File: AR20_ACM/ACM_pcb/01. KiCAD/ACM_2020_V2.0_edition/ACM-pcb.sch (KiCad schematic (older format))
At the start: 32 parts, among them IC1 MCP25625T-E_ML, J1 TC2030-MCP-NL, P1 Conn_02x15_Odd_Even, Q1 Q_PMOS_DMP3099L-13, U1 ATmega328P-AU, U3 NCV890430MW50TXG, Y1 16.0Mhz

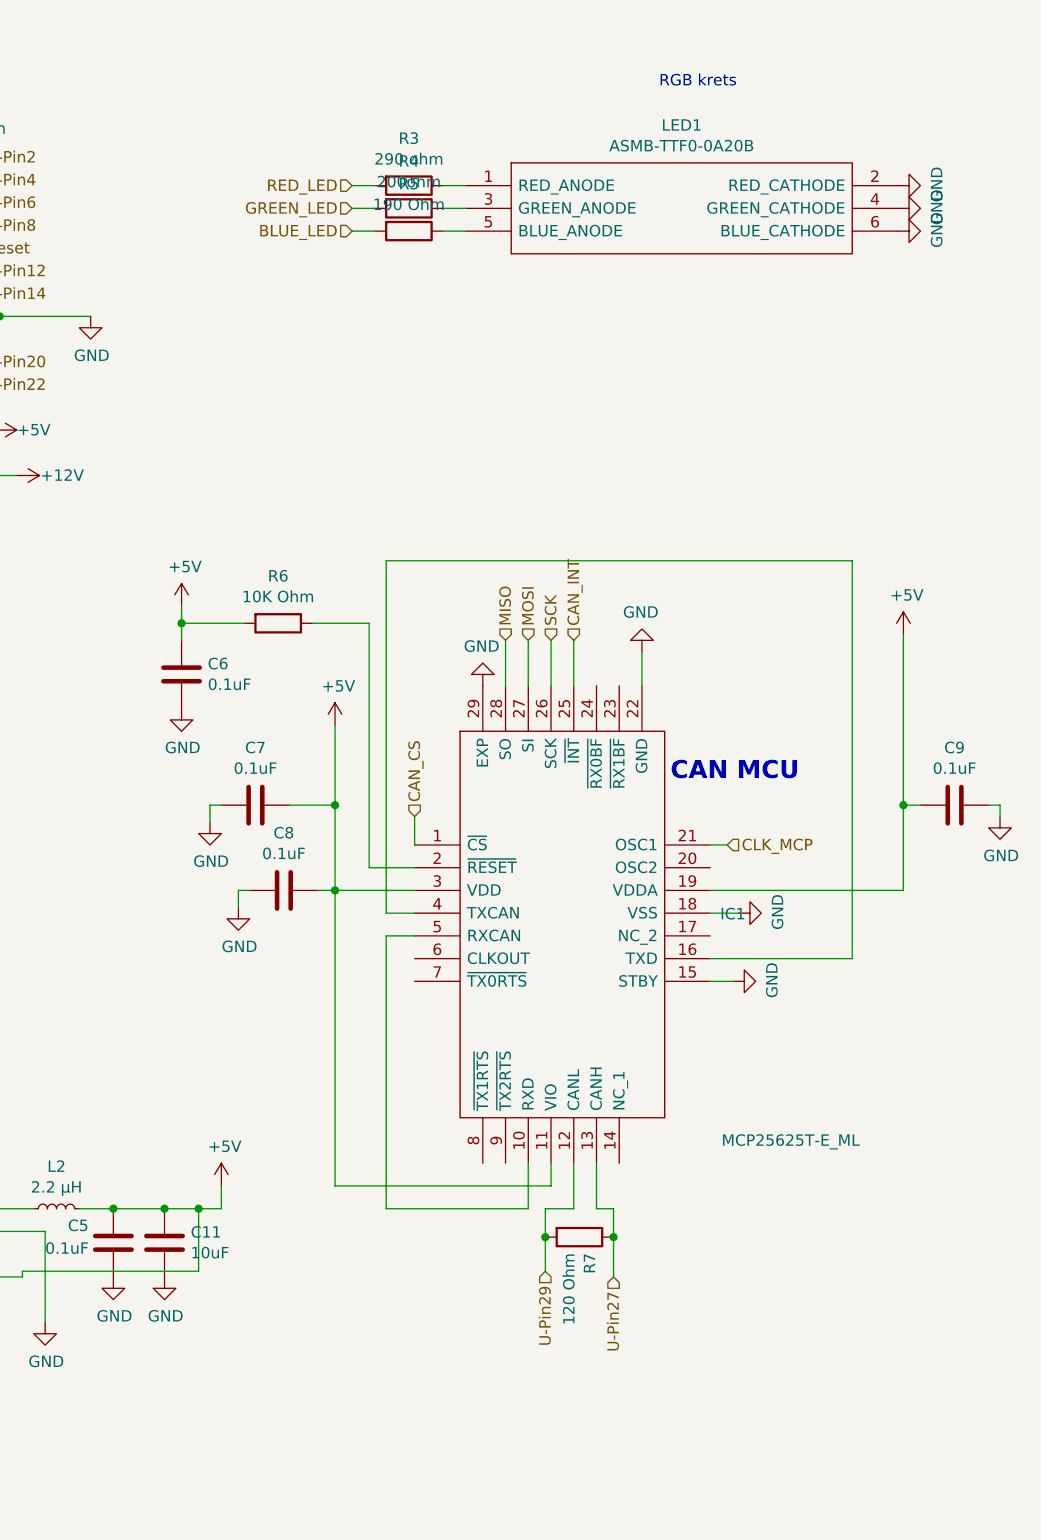
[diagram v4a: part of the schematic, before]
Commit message: NOT COMPLETE V3.0 ACM
This is the beginning of the V3.0 ACM. With added CAN FD transiver and CAN FD controller. 
To fix: 
Chagne CAN FD transciver to a SOCI version 
Place all capacitors in a good location. 
Board cleanup
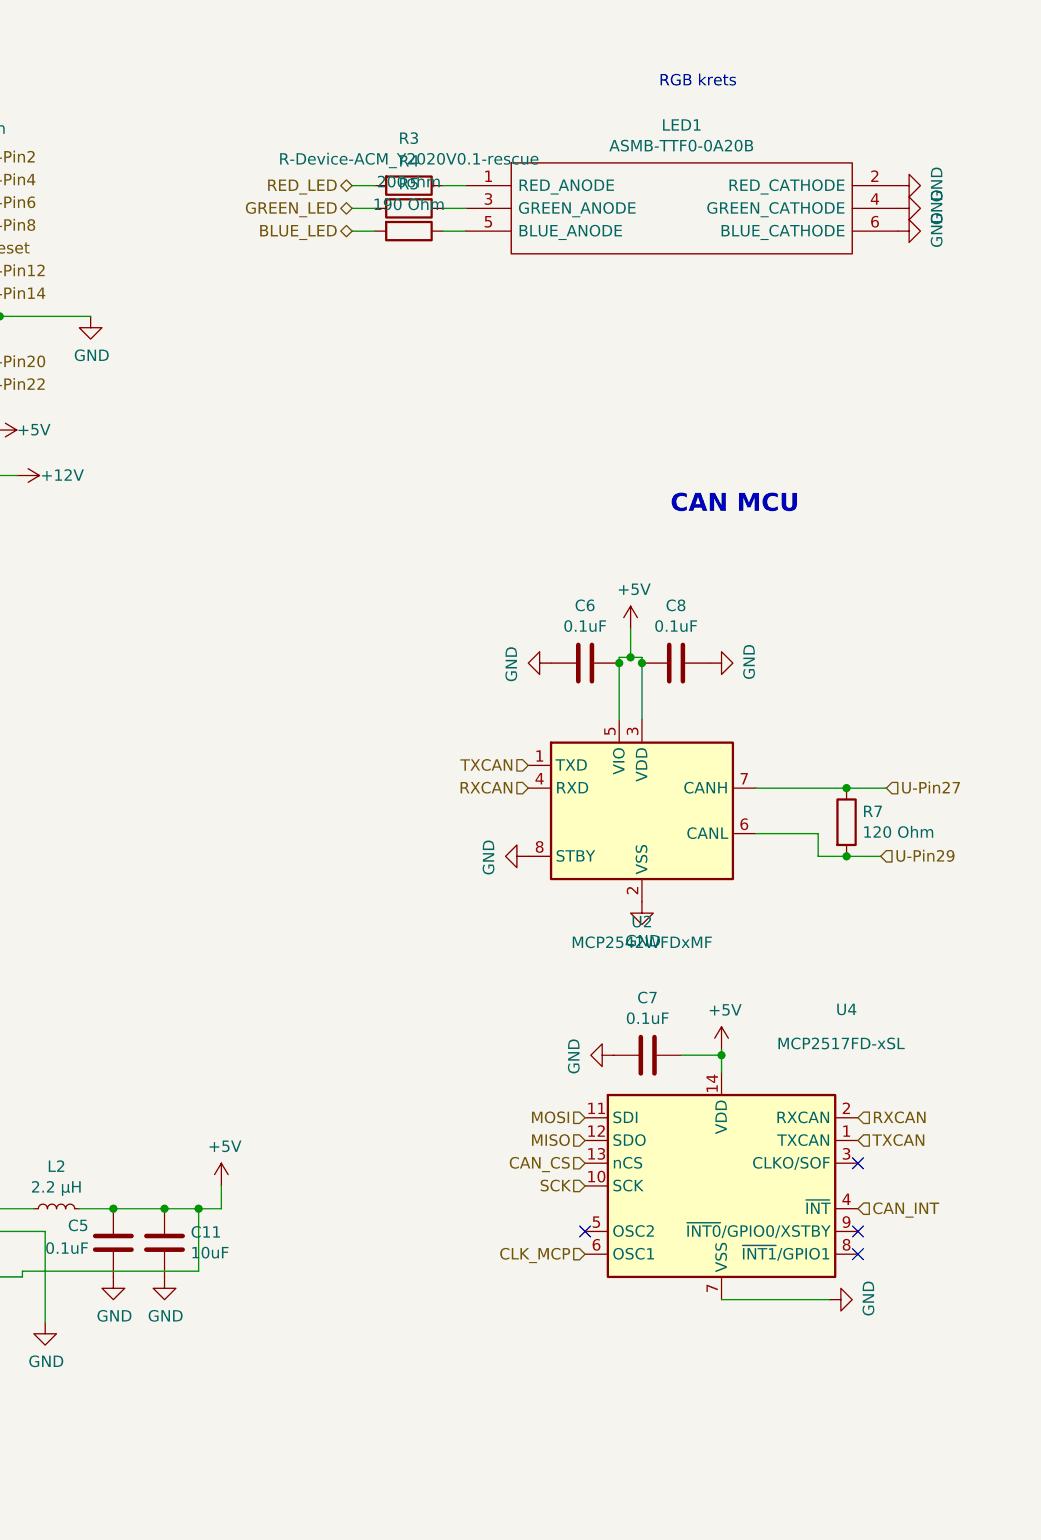
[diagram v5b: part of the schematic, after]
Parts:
- removed C9: 0.1uF, Capacitor_SMD:C_0402_1005Metric, symbol ACM-pcb-rescue:C-Device-ACM_Y2020V0.1-rescue
- removed IC1: MCP25625T-E_ML, ACM_2020_V2:QFN65P600X600X100-29N-D, symbol ACM-pcb-rescue:MCP25625T-E_ML
- removed R6: 10K Ohm, Resistor_SMD:R_0402_1005Metric, symbol ACM-pcb-rescue:R-Device-ACM_Y2020V0.1-rescue
- added U2: MCP2542WFDxMF, Package_DFN_QFN:DFN-8-1EP_3x3mm_P0.65mm_EP1.55x2.4mm, symbol ACM-pcb-rescue:MCP2542WFDxMF
- added U4: MCP2517FD-xSL, ACM_2020_V2:Can_MCP2517FD_SOIC, symbol ACM-pcb-rescue:MCP2517FD-xSL
- R3: value 290 ohm -> R-Device-ACM_Y2020V0.1-rescue
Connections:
- net +5V: now also C8.2, U2.3 (VDD), U2.5 (VIO), U4.14 (VDD); no longer C8.1
- net CAN_CS: now also U4.13 (nCS)
- net CAN_INT: now also U4.4 (~INT)
- net CLK_MCP: now also U4.6 (OSC1)
- net GND: now also C8.1, U2.2 (VSS), U2.8 (STBY), U4.7 (VSS); no longer C8.2
- net MISO: now also U4.12 (SDO)
- net MOSI: now also U4.11 (SDI)
- net SCK: now also U4.10 (SCK)
- net U-Pin27: now also U2.7 (CANH)
- net U-Pin29: now also U2.6 (CANL)
- new net RXCAN: U2.4 (RXD), U4.2 (RXCAN)
- new net TXCAN: U2.1 (TXD), U4.1 (TXCAN)
- no-connect marks 0 -> 4
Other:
- moved on the sheet: R7

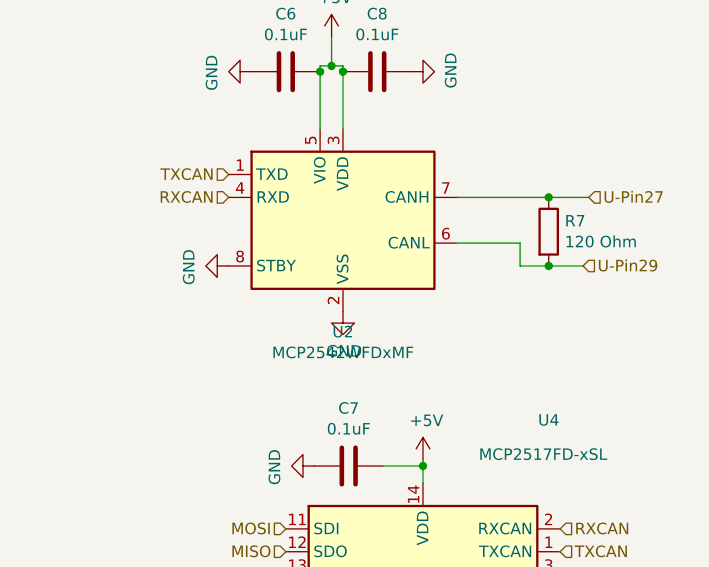
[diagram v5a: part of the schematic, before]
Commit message: ACM 3.0 CAN FD implemented and made SOIC
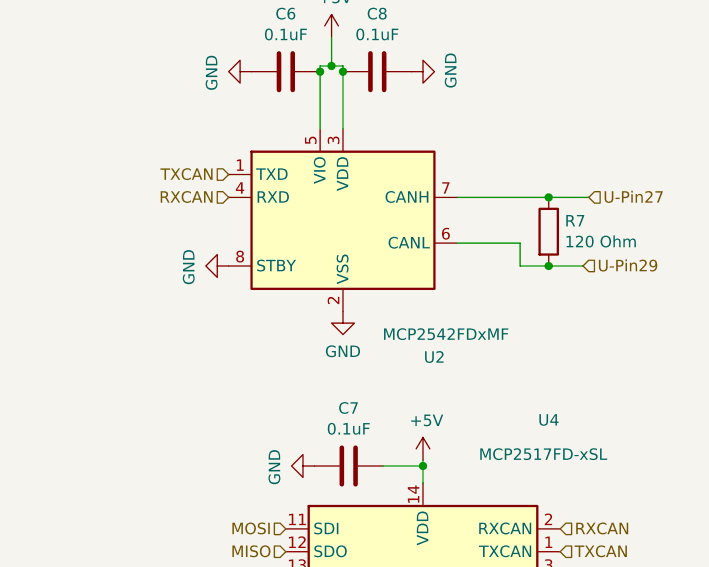
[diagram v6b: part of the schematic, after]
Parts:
- removed U2: MCP2542WFDxMF, Package_DFN_QFN:DFN-8-1EP_3x3mm_P0.65mm_EP1.55x2.4mm, symbol ACM-pcb-rescue:MCP2542WFDxMF
- added U2: MCP2542FDxMF, ACM_2020_V2:SOIC_MCP2542FD, symbol ACM-pcb-rescue:MCP2542FDxMF
- LED1: footprint ASMB-TTF0-0A20B:ASMBTTF00A20B -> ACM_2020_V2:ASMBTTF00A20B
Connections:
- net +5V: now also U2.3 (VDD), U2.5 (VIO)
- net GND: now also U2.2 (VSS), U2.8 (STBY)
- net RXCAN: now also U2.4 (RXD)
- net TXCAN: now also U2.1 (TXD)
- net U-Pin27: now also U2.7 (CANH)
- net U-Pin29: now also U2.6 (CANL)
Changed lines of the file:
@@
 Sheet 1 1
 Title "ACM 2020"
-Date "2019-07-26"
-Rev "A"
+Date "2020-10-03"
+Rev "V3.0"
 Comp "Align Racing UiA"
 Comment1 ""
@@
 Wire Wire Line
 	10450 3950 10625 3950
-Connection ~ 10450 3950
 Wire Wire Line
 	10325 4250 10450 4250
@@
 F 0 "LED1" H 9725 1565 50  0000 C CNN
 F 1 "ASMB-TTF0-0A20B" H 9725 1474 50  0000 C CNN
-F 2 "ASMB-TTF0-0A20B:ASMBTTF00A20B" H 10525 1400 50  0001 L CNN
+F 2 "ACM_2020_V2:ASMBTTF00A20B" H 10525 1400 50  0001 L CNN
 F 3 "https://componentsearchengine.com/Datasheets/1/ASMB-TTF0-0A20B.pdf" H 10525 1300 50  0001 L CNN
 F 4 "BROADCOM LIMITED - ASMB-TTF0-0A20B - LED, RGB, 710/1840/410MCD, PLCC-6" H 10525 1200 50  0001 L CNN "Description"
@@
 Wire Wire Line
 	10325 4150 10325 4250
-Wire Wire Line
-	10050 3950 10450 3950
 $Comp
 L ACM-pcb-rescue:GND-power-ACM_Y2020V0.1-rescue #PWR0104
@@
 P 9550 4450
 F 0 "#PWR0104" H 9550 4200 50  0001 C CNN
-F 1 "GND" H 9555 4277 50  0000 C CNN
+F 1 "GND" H 9550 4275 50  0000 C CNN
 F 2 "" H 9550 4450 50  0001 C CNN
 F 3 "" H 9550 4450 50  0001 C CNN
@@
 $EndComp
 $Comp
-L ACM-pcb-rescue:MCP2542WFDxMF U2
-U 1 1 5F77486A
-P 9550 4050
-F 0 "U2" H 9550 3561 50  0000 C CNN
-F 1 "MCP2542WFDxMF" H 9550 3470 50  0000 C CNN
-F 2 "Package_DFN_QFN:DFN-8-1EP_3x3mm_P0.65mm_EP1.55x2.4mm" H 9550 3550 50  0001 C CIN
-F 3 "http://ww1.microchip.com/downloads/en/DeviceDoc/MCP2542FD-4FD-MCP2542WFD-4WFD-Data-Sheet20005514B.pdf" H 9550 4050 50  0001 C CNN
-	1    9550 4050
-	1    0    0    -1
-$EndComp
-$Comp
 L ACM-pcb-rescue:C-Device-ACM_Y2020V0.1-rescue C7
 U 1 1 5F8944CC
@@
 Wire Wire Line
 	9500 3375 9550 3375
+Wire Wire Line
+	10450 3950 10050 3950
+Connection ~ 10450 3950
+$Comp
+L ACM-pcb-rescue:MCP2542FDxMF U2
+U 1 1 5F796A7A
+P 9550 4050
+F 0 "U2" H 9950 3450 50  0000 C CNN
+F 1 "MCP2542FDxMF" H 10000 3550 50  0000 C CNN
+F 2 "ACM_2020_V2:SOIC_MCP2542FD" H 9550 3550 50  0001 C CIN
+F 3 "http://ww1.microchip.com/downloads/en/DeviceDoc/MCP2542FD-4FD-MCP2542WFD-4WFD-Data-Sheet20005514B.pdf" H 9550 4050 50  0001 C CNN
+	1    9550 4050
+	1    0    0    -1
+$EndComp
 $EndSCHEMATC

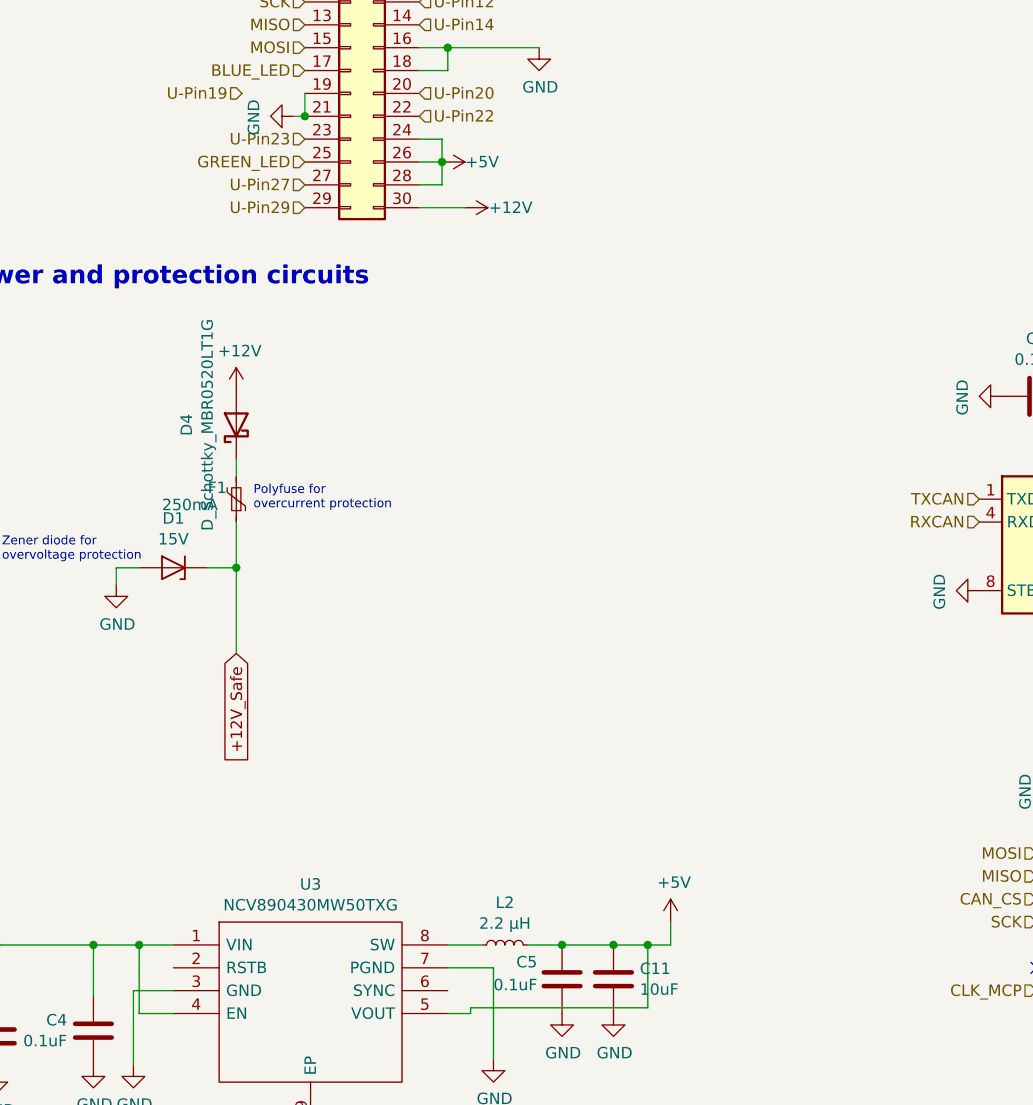
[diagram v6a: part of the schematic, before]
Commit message: Added Zener diode between 5V and ground
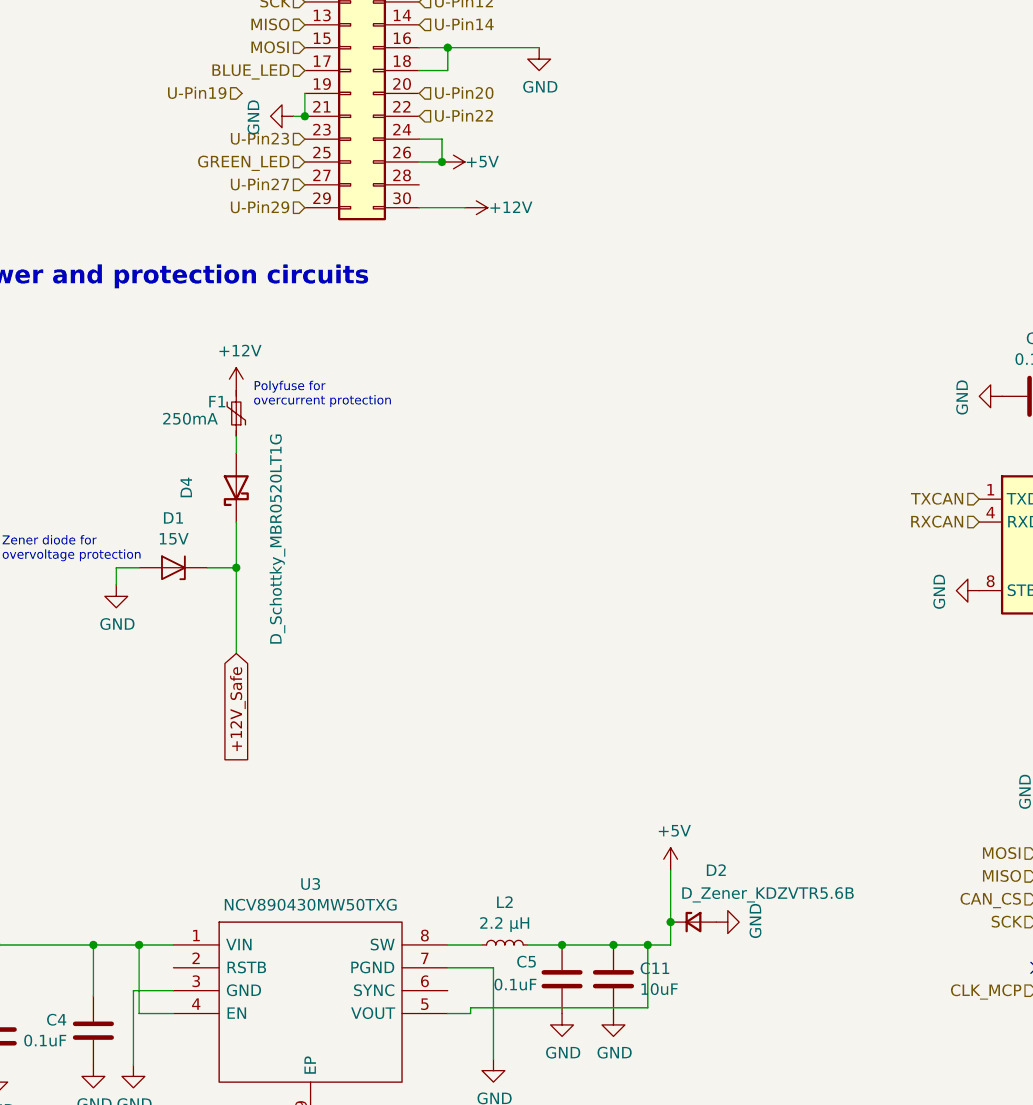
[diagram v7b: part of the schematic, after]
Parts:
- added D2: D_Zener_KDZVTR5.6B, ACM_2020_V2:D_Zener_KDZV5.6B_SOD-123, symbol ACM-pcb-rescue:D_Zener_KDZVTR5.6B
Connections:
- net +12V: now also F1.2; no longer D4.2 (A)
- net +12V_Safe: now also D4.1 (K); no longer F1.1
- net +5V: now also D2.1 (K); no longer P1.28 (Pin_28)
- net GND: now also D2.2 (A)
- new net: D4.2 (A), F1.1
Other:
- moved on the sheet: D4, F1
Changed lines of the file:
@@
 L ACM-pcb-rescue:Polyfuse_Small-Device-ACM_Y2020V0.1-rescue F1
 U 1 1 5D45109C
-P 5800 3850
-F 0 "F1" H 5925 3800 50  0000 R CNN
-F 1 "250mA" H 6125 3875 50  0000 R CNN
-F 2 "Fuse:Fuse_0603_1608Metric" H 5850 3650 50  0001 L CNN
-F 3 "http://www.farnell.com/datasheets/2571643.pdf?_ga=2.98152344.620744209.1564174328-1415930916.1560114588&_gac=1.180027990.1564075292.CjwKCAjwpuXpBRAAEiwAyRRPgXwHZ1wF4xXBoNI_FJEvoVORJn7NbJB9jjbidsg8_qDnlLi_44u6wRoCV2MQAvD_BwE" H 5800 3850 50  0001 C CNN
-F 4 "https://no.farnell.com/bel-fuse-circuit-protection/0zcm0010ff2g/fuse-resettable-ptc-15vdc-0-1a/dp/2834930" H 5800 3850 50  0001 C CNN "Farnell"
-	1    5800 3850
+P 5800 3475
+F 0 "F1" H 5925 3425 50  0000 R CNN
+F 1 "250mA" H 6125 3500 50  0000 R CNN
+F 2 "Fuse:Fuse_0603_1608Metric" H 5850 3275 50  0001 L CNN
+F 3 "http://www.farnell.com/datasheets/2571643.pdf?_ga=2.98152344.620744209.1564174328-1415930916.1560114588&_gac=1.180027990.1564075292.CjwKCAjwpuXpBRAAEiwAyRRPgXwHZ1wF4xXBoNI_FJEvoVORJn7NbJB9jjbidsg8_qDnlLi_44u6wRoCV2MQAvD_BwE" H 5800 3475 50  0001 C CNN
+F 4 "https://no.farnell.com/bel-fuse-circuit-protection/0zcm0010ff2g/fuse-resettable-ptc-15vdc-0-1a/dp/2834930" H 5800 3475 50  0001 C CNN "Farnell"
+	1    5800 3475
 	-1   0    0    1
 $EndComp
@@
 Text Notes 4775 4125 0    39   ~ 0
 Zener diode for\novervoltage protection
-Text Notes 5875 3900 0    39   ~ 0
+Text Notes 5875 3450 0    39   ~ 0
 Polyfuse for\novercurrent protection
 $Comp
@@
 Text Notes 950  4075 0    50   ~ 0
 Trenger flere Decupling Caps?
-Wire Wire Line
-	5800 3675 5800 3750
 Wire Wire Line
 	5675 4150 5800 4150
@@
 L ACM-pcb-rescue:+5V-power-ACM_Y2020V0.1-rescue #PWR022
 U 1 1 5D4DE85A
-P 7700 5700
-F 0 "#PWR022" H 7700 5550 50  0001 C CNN
-F 1 "+5V" H 7715 5873 50  0000 C CNN
-F 2 "" H 7700 5700 50  0001 C CNN
-F 3 "" H 7700 5700 50  0001 C CNN
-	1    7700 5700
+P 7700 5475
+F 0 "#PWR022" H 7700 5325 50  0001 C CNN
+F 1 "+5V" H 7715 5648 50  0000 C CNN
+F 2 "" H 7700 5475 50  0001 C CNN
+F 3 "" H 7700 5475 50  0001 C CNN
+	1    7700 5475
 	1    0    0    -1
 $EndComp
@@
 	6600 2575 6800 2575
 Wire Wire Line
-	6600 2475 6700 2475
-Wire Wire Line
-	6700 2475 6700 2375
-Wire Wire Line
 	6100 2075 6100 2175
 Wire Wire Line
@@
 L ACM-pcb-rescue:D_Schottky_MBR0520LT1G D4
 U 1 1 5F71C208
-P 5800 3525
-F 0 "D4" H 5800 3742 50  0000 C CNN
-F 1 "D_Schottky_MBR0520LT1G" H 5800 3651 50  0000 C CNN
-F 2 "ACM_2020_V2:D_schotky_MBR0520LT1G" H 5800 3525 50  0001 C CNN
-F 3 "~" H 5800 3525 50  0001 C CNN
-	1    5800 3525
+P 5800 3800
+F 0 "D4" H 5800 4017 50  0000 C CNN
+F 1 "D_Schottky_MBR0520LT1G" H 5575 3625 50  0000 C CNN
+F 2 "ACM_2020_V2:D_schotky_MBR0520LT1G" H 5800 3800 50  0001 C CNN
+F 3 "~" H 5800 3800 50  0001 C CNN
+	1    5800 3800
 	0    -1   -1   0
 $EndComp
@@
 	1    0    0    -1
 $EndComp
+$Comp
+L ACM-pcb-rescue:D_Zener_KDZVTR5.6B D2
+U 1 1 5F86EBF9
+P 7800 5700
+F 0 "D2" H 7900 5925 50  0000 C CNN
+F 1 "D_Zener_KDZVTR5.6B" H 8125 5825 50  0000 C CNN
+F 2 "ACM_2020_V2:D_Zener_KDZV5.6B_SOD-123" V 7800 5700 50  0001 C CNN
+F 3 "~" V 7800 5700 50  0001 C CNN
+	1    7800 5700
+	1    0    0    -1
+$EndComp
+Wire Wire Line
+	7700 5475 7700 5700
+Connection ~ 7700 5700
+$Comp
+L ACM-pcb-rescue:GND-power-ACM_Y2020V0.1-rescue #PWR023
+U 1 1 5F8750C3
+P 7900 5700
+F 0 "#PWR023" H 7900 5450 50  0001 C CNN
+F 1 "GND" H 7905 5527 50  0000 C CNN
+F 2 "" H 7900 5700 50  0001 C CNN
+F 3 "" H 7900 5700 50  0001 C CNN
+	1    7900 5700
+	0    -1   -1   0
+$EndComp
+Wire Wire Line
+	5800 3575 5800 3650
 $EndSCHEMATC
